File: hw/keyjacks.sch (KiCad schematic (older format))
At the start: 43 parts

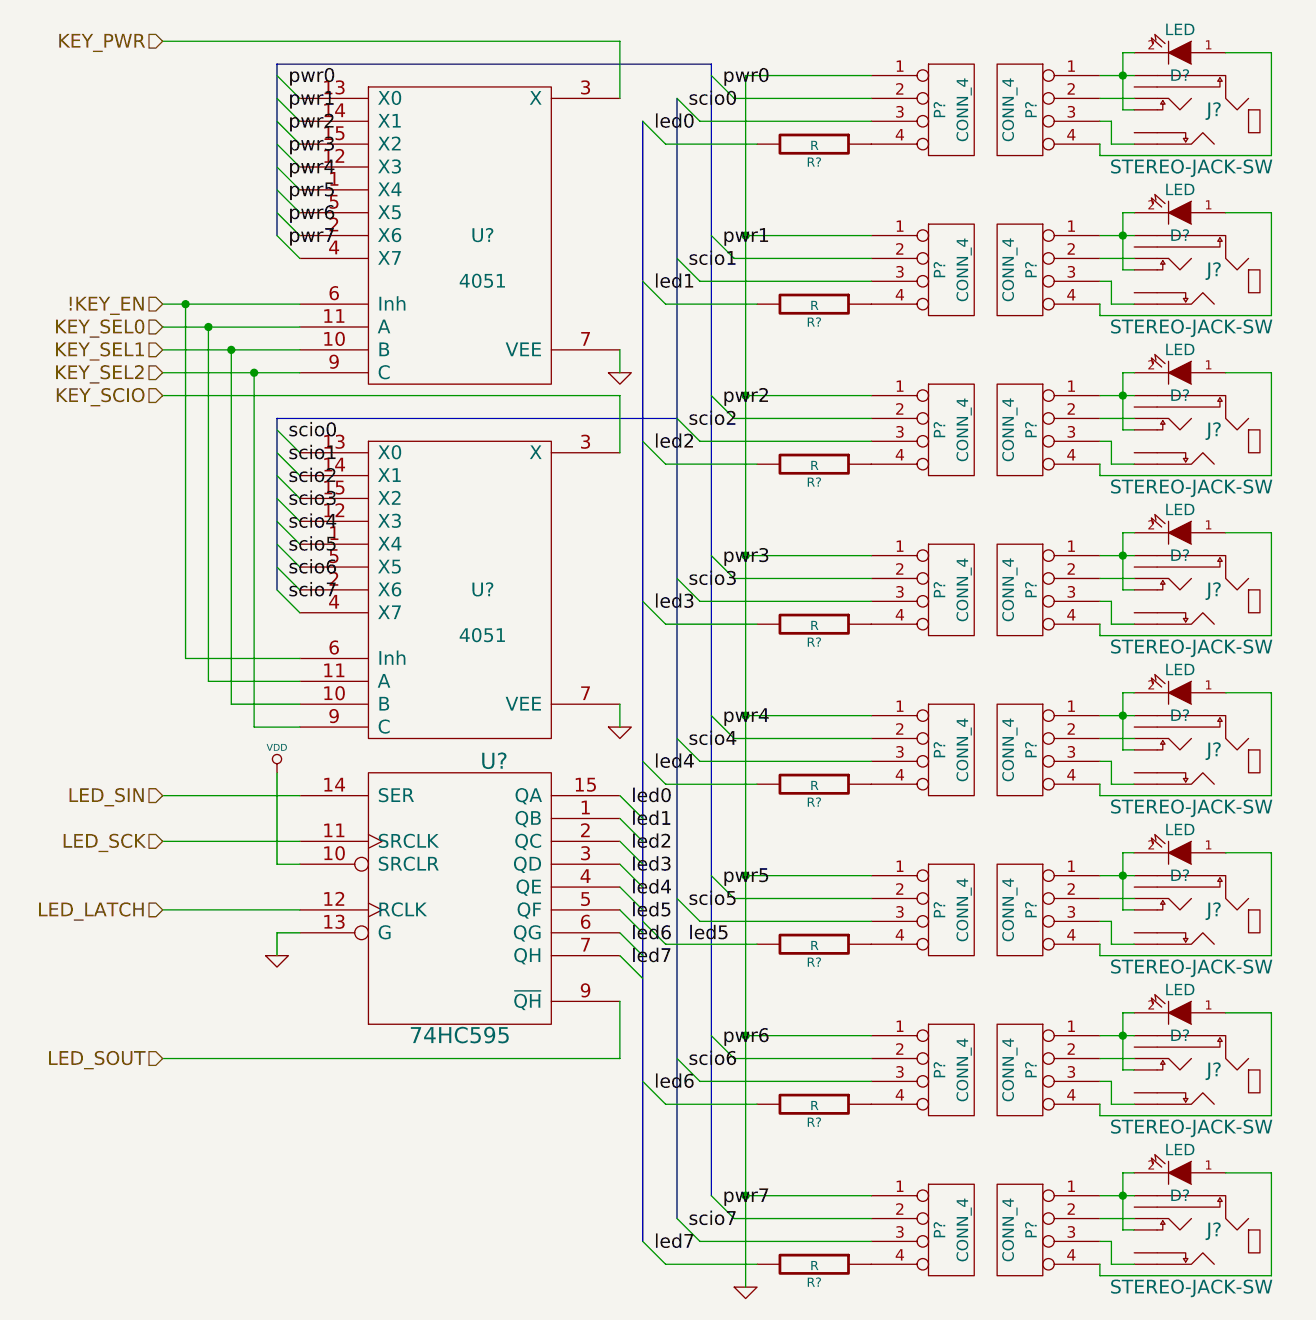
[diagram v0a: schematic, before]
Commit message: Add decaps, make schematic fit for PCB, start PCB
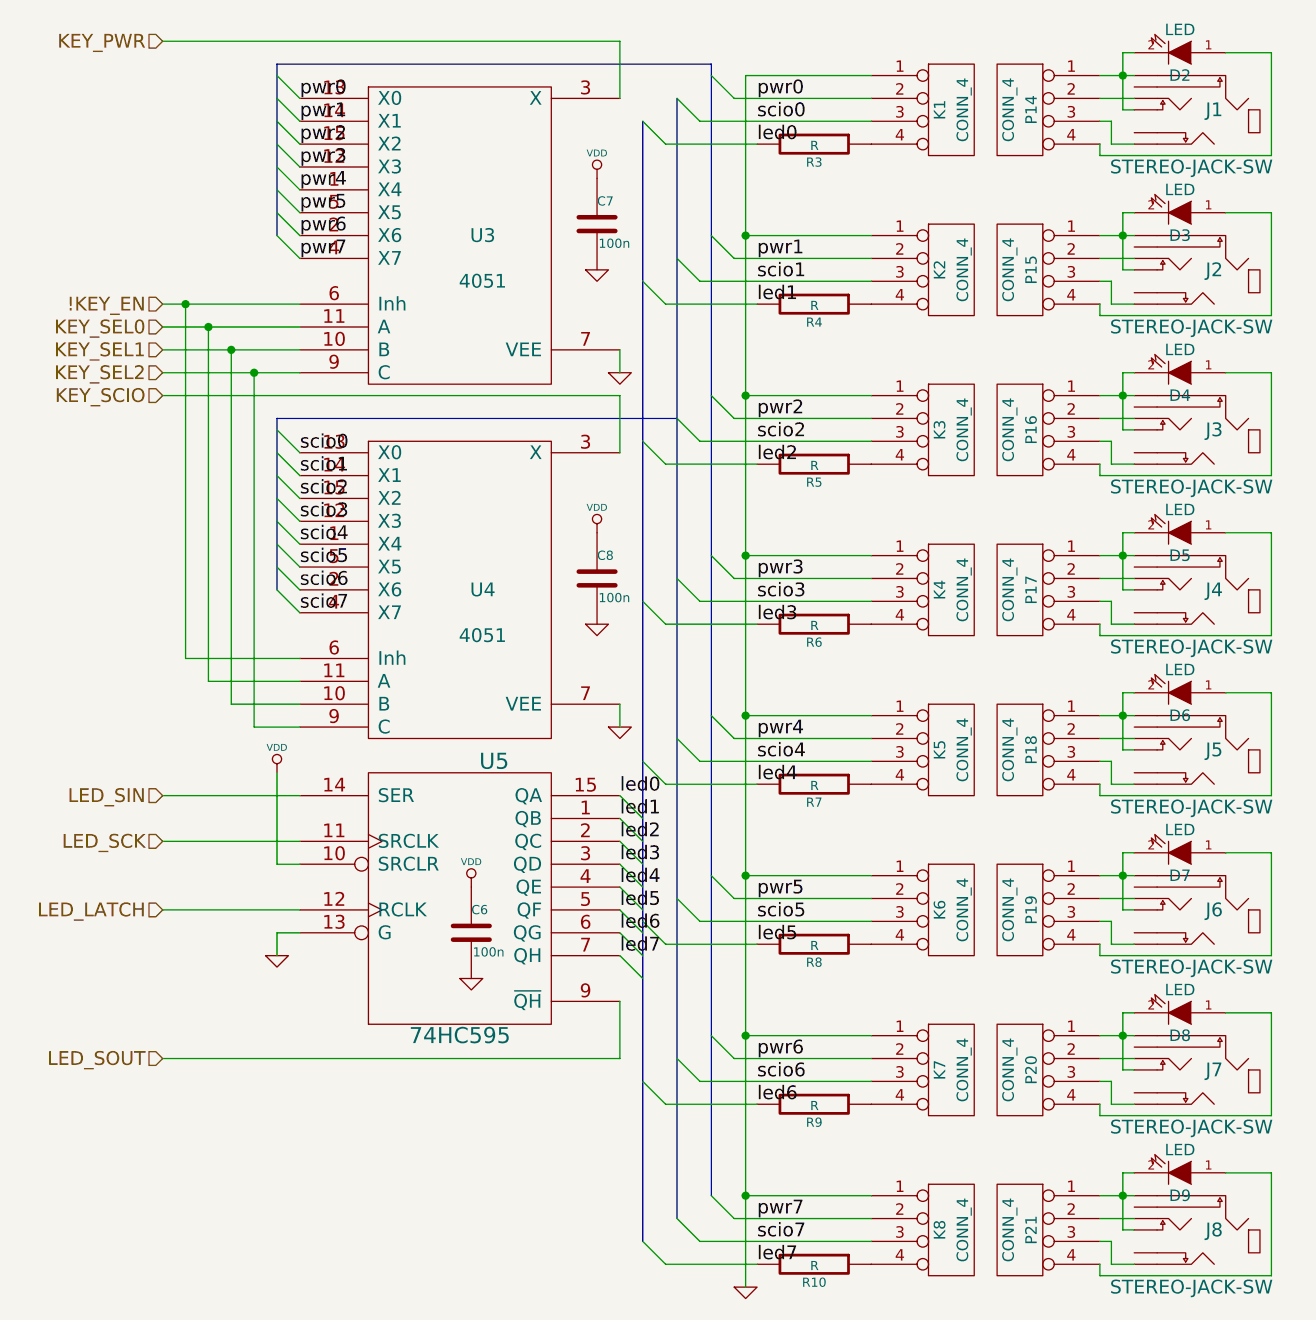
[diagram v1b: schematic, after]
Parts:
- added C6, C7, C8: 100n, ~, symbol C
- gave numbers to parts that had none: 43
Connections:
- net GND: now also C6.2, C7.2, C8.2
- net VDD: now also C6.1, C7.1, C8.1
- net led0: now also R3.2, U5.15 (QA)
- net led1: now also R4.2, U5.1 (QB)
- net led2: now also R5.2, U5.2 (QC)
- net led3: now also R6.2, U5.3 (QD)
- net led4: now also R7.2, U5.4 (QE)
- net led5: now also U5.5 (QF)
- net led6: now also R9.2, U5.6 (QG)
- net led7: now also R10.2, U5.7 (QH)
- net pwr0: now also K1.2 (P2), U3.13 (X0)
- net pwr1: now also K2.2 (P2), U3.14 (X1)
- net pwr2: now also K3.2 (P2), U3.15 (X2)
- net pwr3: now also K4.2 (P2), U3.12 (X3)
- net pwr4: now also K5.2 (P2), U3.1 (X4)
- net pwr5: now also K6.2 (P2), U3.5 (X5)
- net pwr6: now also K7.2 (P2), U3.2 (X6)
- net pwr7: now also K8.2 (P2), U3.4 (X7)
- net scio0: now also K1.3 (P3), U4.13 (X0)
- net scio1: now also K2.3 (P3), U4.14 (X1)
- net scio2: now also K3.3 (P3), U4.15 (X2)
- net scio3: now also K4.3 (P3), U4.12 (X3)
- net scio4: now also K5.3 (P3), U4.1 (X4)
- net scio5: now also K6.3 (P3), U4.5 (X5)
- net scio6: now also K7.3 (P3), U4.2 (X6)
- net scio7: now also K8.3 (P3), U4.4 (X7)
- net at J1.~ (TIP-SW): now also P14.3 (P3)

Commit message: Change LED pin order, complete routing of key jacks
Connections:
- net led0: now also U5.7 (QH); no longer U5.15 (QA)
- net led1: now also U5.6 (QG); no longer U5.1 (QB)
- net led2: now also U5.5 (QF); no longer U5.2 (QC)
- net led3: now also U5.4 (QE); no longer U5.3 (QD)
- net led4: now also U5.3 (QD); no longer U5.4 (QE)
- net led5: now also U5.2 (QC); no longer U5.5 (QF)
- net led6: now also U5.1 (QB); no longer U5.6 (QG)
- net led7: now also U5.15 (QA); no longer U5.7 (QH)
- net at J1.~ (TIP-SW): now also P14.3 (P3)
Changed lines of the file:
@@
 Sheet 2 2
 Title ""
-Date "13 nov 2013"
+Date "15 nov 2013"
 Rev ""
 Comp ""
@@
 Text Label 2650 3750 0    60   ~ 0
 scio7
+Text Label 4050 5250 0    60   ~ 0
+led0
+Text Label 4050 5150 0    60   ~ 0
+led1
+Text Label 4050 5050 0    60   ~ 0
+led2
+Text Label 4050 4950 0    60   ~ 0
+led3
+Text Label 4050 4850 0    60   ~ 0
+led4
+Text Label 4050 4750 0    60   ~ 0
+led5
+Text Label 4050 4650 0    60   ~ 0
+led6
 Text Label 4050 4550 0    60   ~ 0
-led0
-Text Label 4050 4650 0    60   ~ 0
-led1
-Text Label 4050 4750 0    60   ~ 0
-led2
-Text Label 4050 4850 0    60   ~ 0
-led3
-Text Label 4050 4950 0    60   ~ 0
-led4
-Text Label 4050 5050 0    60   ~ 0
-led5
-Text Label 4050 5150 0    60   ~ 0
-led6
-Text Label 4050 5250 0    60   ~ 0
 led7
 Text Label 4650 1500 0    60   ~ 0

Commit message: Routed all signals, only VDD/GND remaining
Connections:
- net at J1.~ (TIP-SW): now also P14.3 (P3)
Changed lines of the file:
@@
 Sheet 2 2
 Title ""
-Date "15 nov 2013"
+Date "16 nov 2013"
 Rev ""
 Comp ""
@@
 	4150 6500 4250 6600
 $Comp
-L GND #PWR41
+L GND #PWR036
 U 1 1 526401CD
 P 4600 6700
-F 0 "#PWR41" H 4600 6700 30  0001 C CNN
+F 0 "#PWR036" H 4600 6700 30  0001 C CNN
 F 1 "GND" H 4600 6630 30  0001 C CNN
 F 2 "" H 4600 6700 60  0000 C CNN
@@
 	2550 1350 2550 2100
 $Comp
-L GND #PWR39
+L GND #PWR037
 U 1 1 526402DC
 P 4050 2700
-F 0 "#PWR39" H 4050 2700 30  0001 C CNN
+F 0 "#PWR037" H 4050 2700 30  0001 C CNN
 F 1 "GND" H 4050 2630 30  0001 C CNN
 F 2 "" H 4050 2700 60  0000 C CNN
@@
 	4050 2700 4050 2600
 $Comp
-L GND #PWR40
+L GND #PWR038
 U 1 1 526402E3
 P 4050 4250
-F 0 "#PWR40" H 4050 4250 30  0001 C CNN
+F 0 "#PWR038" H 4050 4250 30  0001 C CNN
 F 1 "GND" H 4050 4180 30  0001 C CNN
 F 2 "" H 4050 4250 60  0000 C CNN
@@
 	2550 5150 2550 5250
 $Comp
-L GND #PWR32
+L GND #PWR039
 U 1 1 526402FF
 P 2550 5250
-F 0 "#PWR32" H 2550 5250 30  0001 C CNN
+F 0 "#PWR039" H 2550 5250 30  0001 C CNN
 F 1 "GND" H 2550 5180 30  0001 C CNN
 F 2 "" H 2550 5250 60  0000 C CNN
@@
 $EndComp
 $Comp
-L VDD #PWR31
+L VDD #PWR040
 U 1 1 52640305
 P 2550 4450
-F 0 "#PWR31" H 2550 4550 30  0001 C CNN
+F 0 "#PWR040" H 2550 4550 30  0001 C CNN
 F 1 "VDD" H 2550 4560 30  0000 C CNN
 F 2 "" H 2550 4450 60  0000 C CNN
@@
 	6250 6450 6300 6450
 $Comp
-L VDD #PWR35
+L VDD #PWR041
 U 1 1 5283F3B5
 P 3950 1850
-F 0 "#PWR35" H 3950 1950 30  0001 C CNN
+F 0 "#PWR041" H 3950 1950 30  0001 C CNN
 F 1 "VDD" H 3950 1960 30  0000 C CNN
 F 2 "" H 3950 1850 60  0000 C CNN
@@
 $EndComp
 $Comp
-L GND #PWR36
+L GND #PWR042
 U 1 1 5283F3BB
 P 3950 2250
-F 0 "#PWR36" H 3950 2250 30  0001 C CNN
+F 0 "#PWR042" H 3950 2250 30  0001 C CNN
 F 1 "GND" H 3950 2180 30  0001 C CNN
 F 2 "" H 3950 2250 60  0000 C CNN
@@
 $EndComp
 $Comp
-L VDD #PWR37
+L VDD #PWR043
 U 1 1 5283F3C7
 P 3950 3400
-F 0 "#PWR37" H 3950 3500 30  0001 C CNN
+F 0 "#PWR043" H 3950 3500 30  0001 C CNN
 F 1 "VDD" H 3950 3510 30  0000 C CNN
 F 2 "" H 3950 3400 60  0000 C CNN
@@
 $EndComp
 $Comp
-L GND #PWR38
+L GND #PWR044
 U 1 1 5283F3CD
 P 3950 3800
-F 0 "#PWR38" H 3950 3800 30  0001 C CNN
+F 0 "#PWR044" H 3950 3800 30  0001 C CNN
 F 1 "GND" H 3950 3730 30  0001 C CNN
 F 2 "" H 3950 3800 60  0000 C CNN
@@
 $EndComp
 $Comp
-L VDD #PWR33
+L VDD #PWR045
 U 1 1 5283F3D9
 P 3400 4950
-F 0 "#PWR33" H 3400 5050 30  0001 C CNN
+F 0 "#PWR045" H 3400 5050 30  0001 C CNN
 F 1 "VDD" H 3400 5060 30  0000 C CNN
 F 2 "" H 3400 4950 60  0000 C CNN
@@
 $EndComp
 $Comp
-L GND #PWR34
+L GND #PWR046
 U 1 1 5283F3DF
 P 3400 5350
-F 0 "#PWR34" H 3400 5350 30  0001 C CNN
+F 0 "#PWR046" H 3400 5350 30  0001 C CNN
 F 1 "GND" H 3400 5280 30  0001 C CNN
 F 2 "" H 3400 5350 60  0000 C CNN

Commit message: Yeah, so I had the board reversed -.-   Once more with feeling.
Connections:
- net led0: now also U5.15 (QA); no longer U5.7 (QH)
- net led1: now also U5.1 (QB); no longer U5.6 (QG)
- net led2: now also U5.2 (QC); no longer U5.5 (QF)
- net led3: now also U5.3 (QD); no longer U5.4 (QE)
- net led4: now also U5.4 (QE); no longer U5.3 (QD)
- net led5: now also U5.5 (QF); no longer U5.2 (QC)
- net led6: now also U5.6 (QG); no longer U5.1 (QB)
- net led7: now also U5.7 (QH); no longer U5.15 (QA)
- net at J1.~ (TIP-SW): now also P14.3 (P3)
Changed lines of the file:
@@
 Sheet 2 2
 Title ""
-Date "16 nov 2013"
+Date "17 nov 2013"
 Rev ""
 Comp ""
@@
 Text Label 2650 3750 0    60   ~ 0
 scio7
+Text Label 4050 4550 0    60   ~ 0
+led0
+Text Label 4050 4650 0    60   ~ 0
+led1
+Text Label 4050 4750 0    60   ~ 0
+led2
+Text Label 4050 4850 0    60   ~ 0
+led3
+Text Label 4050 4950 0    60   ~ 0
+led4
+Text Label 4050 5050 0    60   ~ 0
+led5
+Text Label 4050 5150 0    60   ~ 0
+led6
 Text Label 4050 5250 0    60   ~ 0
-led0
-Text Label 4050 5150 0    60   ~ 0
-led1
-Text Label 4050 5050 0    60   ~ 0
-led2
-Text Label 4050 4950 0    60   ~ 0
-led3
-Text Label 4050 4850 0    60   ~ 0
-led4
-Text Label 4050 4750 0    60   ~ 0
-led5
-Text Label 4050 4650 0    60   ~ 0
-led6
-Text Label 4050 4550 0    60   ~ 0
 led7
 Text Label 4650 1500 0    60   ~ 0

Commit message: Assign LED resistor values, change some labels for readability
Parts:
- R10, R3, R4, R5, R6, R7, R8, R9: value R -> 270
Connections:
- net at J1.~ (TIP-SW): now also P14.3 (P3)
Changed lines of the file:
@@
 Sheet 2 2
 Title ""
-Date "17 nov 2013"
+Date "1 dec 2013"
 Rev ""
 Comp ""
@@
 P 4900 6600
 F 0 "R10" V 4980 6600 40  0000 C CNN
-F 1 "R" V 4907 6601 40  0000 C CNN
+F 1 "270" V 4907 6601 40  0000 C CNN
 F 2 "~" V 4830 6600 30  0000 C CNN
 F 3 "~" H 4900 6600 30  0000 C CNN
@@
 P 4900 5900
 F 0 "R9" V 4980 5900 40  0000 C CNN
-F 1 "R" V 4907 5901 40  0000 C CNN
+F 1 "270" V 4907 5901 40  0000 C CNN
 F 2 "~" V 4830 5900 30  0000 C CNN
 F 3 "~" H 4900 5900 30  0000 C CNN
@@
 P 4900 5200
 F 0 "R8" V 4980 5200 40  0000 C CNN
-F 1 "R" V 4907 5201 40  0000 C CNN
+F 1 "270" V 4907 5201 40  0000 C CNN
 F 2 "~" V 4830 5200 30  0000 C CNN
 F 3 "~" H 4900 5200 30  0000 C CNN
@@
 P 4900 4500
 F 0 "R7" V 4980 4500 40  0000 C CNN
-F 1 "R" V 4907 4501 40  0000 C CNN
+F 1 "270" V 4907 4501 40  0000 C CNN
 F 2 "~" V 4830 4500 30  0000 C CNN
 F 3 "~" H 4900 4500 30  0000 C CNN
@@
 P 4900 3800
 F 0 "R6" V 4980 3800 40  0000 C CNN
-F 1 "R" V 4907 3801 40  0000 C CNN
+F 1 "270" V 4907 3801 40  0000 C CNN
 F 2 "~" V 4830 3800 30  0000 C CNN
 F 3 "~" H 4900 3800 30  0000 C CNN
@@
 P 4900 3100
 F 0 "R5" V 4980 3100 40  0000 C CNN
-F 1 "R" V 4907 3101 40  0000 C CNN
+F 1 "270" V 4907 3101 40  0000 C CNN
 F 2 "~" V 4830 3100 30  0000 C CNN
 F 3 "~" H 4900 3100 30  0000 C CNN
@@
 P 4900 2400
 F 0 "R4" V 4980 2400 40  0000 C CNN
-F 1 "R" V 4907 2401 40  0000 C CNN
+F 1 "270" V 4907 2401 40  0000 C CNN
 F 2 "~" V 4830 2400 30  0000 C CNN
 F 3 "~" H 4900 2400 30  0000 C CNN
@@
 P 4900 1700
 F 0 "R3" V 4980 1700 40  0000 C CNN
-F 1 "R" V 4907 1701 40  0000 C CNN
+F 1 "270" V 4907 1701 40  0000 C CNN
 F 2 "~" V 4830 1700 30  0000 C CNN
 F 3 "~" H 4900 1700 30  0000 C CNN
